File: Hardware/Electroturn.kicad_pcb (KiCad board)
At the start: 2 copper layers, 100 x 100 mm, 10 parts, among them J1 Encoder Terminal, J2 Stepper Motor Terminal, U1 Teensy 4.0, U2 MCP23017_SP

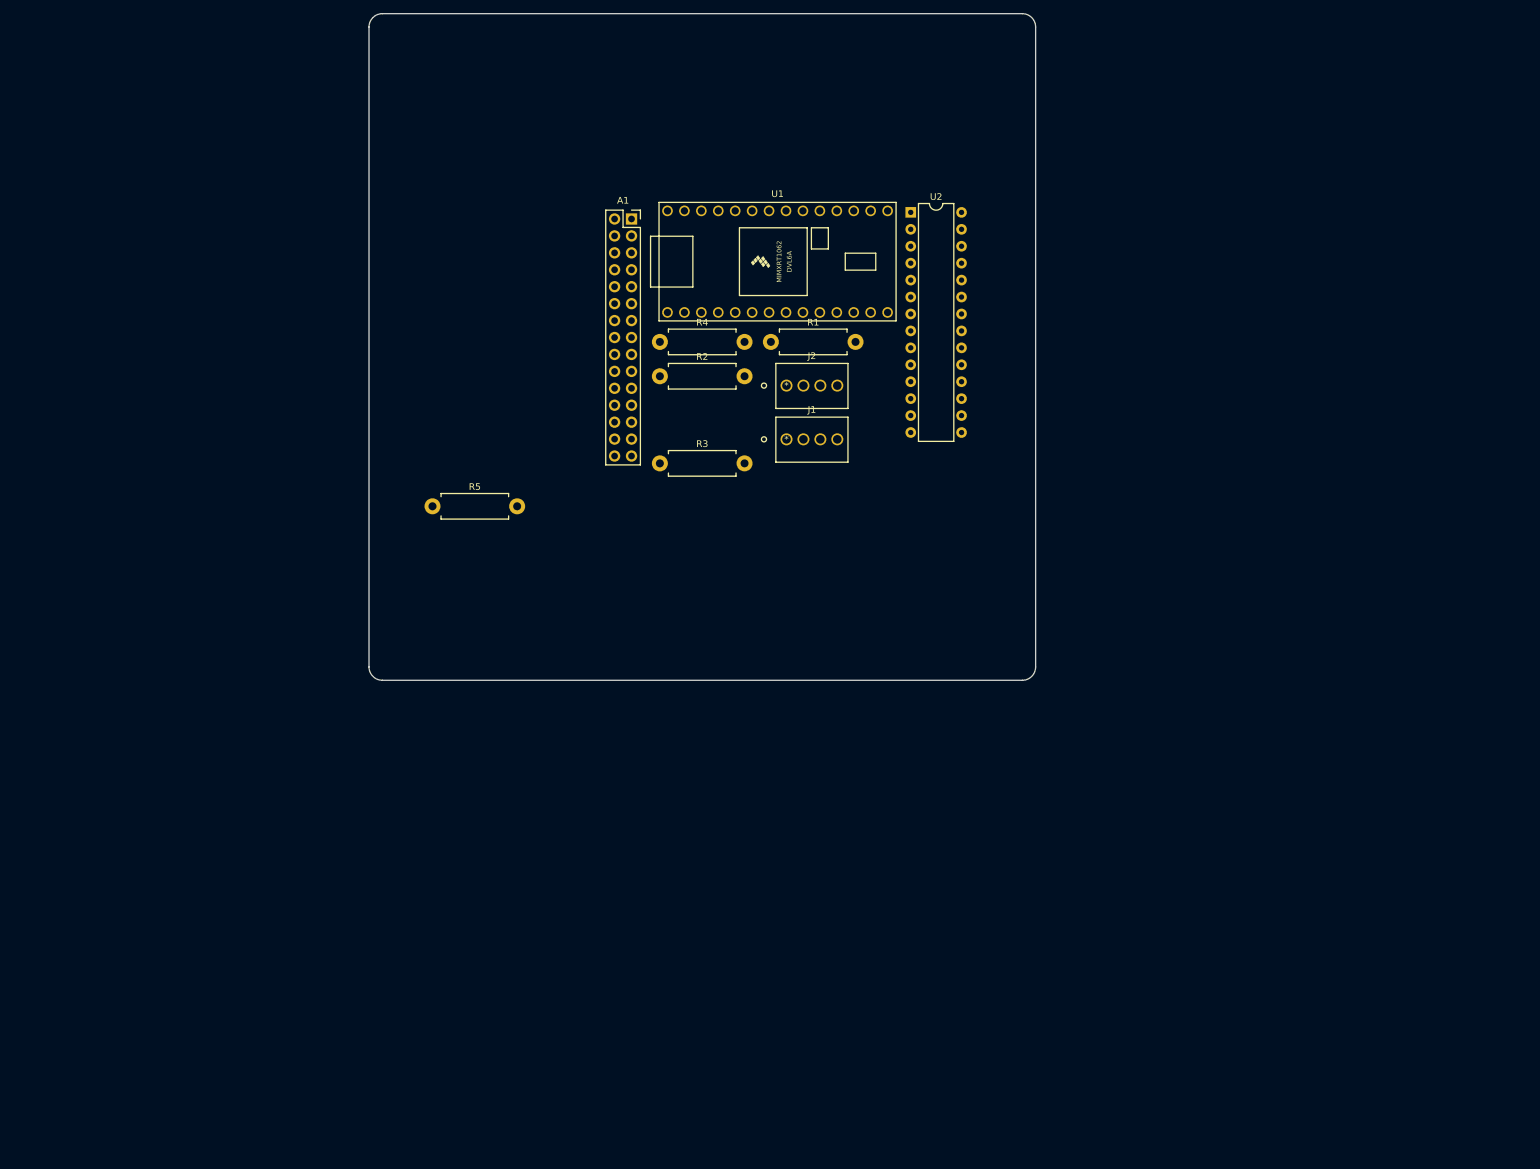
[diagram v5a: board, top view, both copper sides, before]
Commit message: Footprint housekeeping, updating PCB components
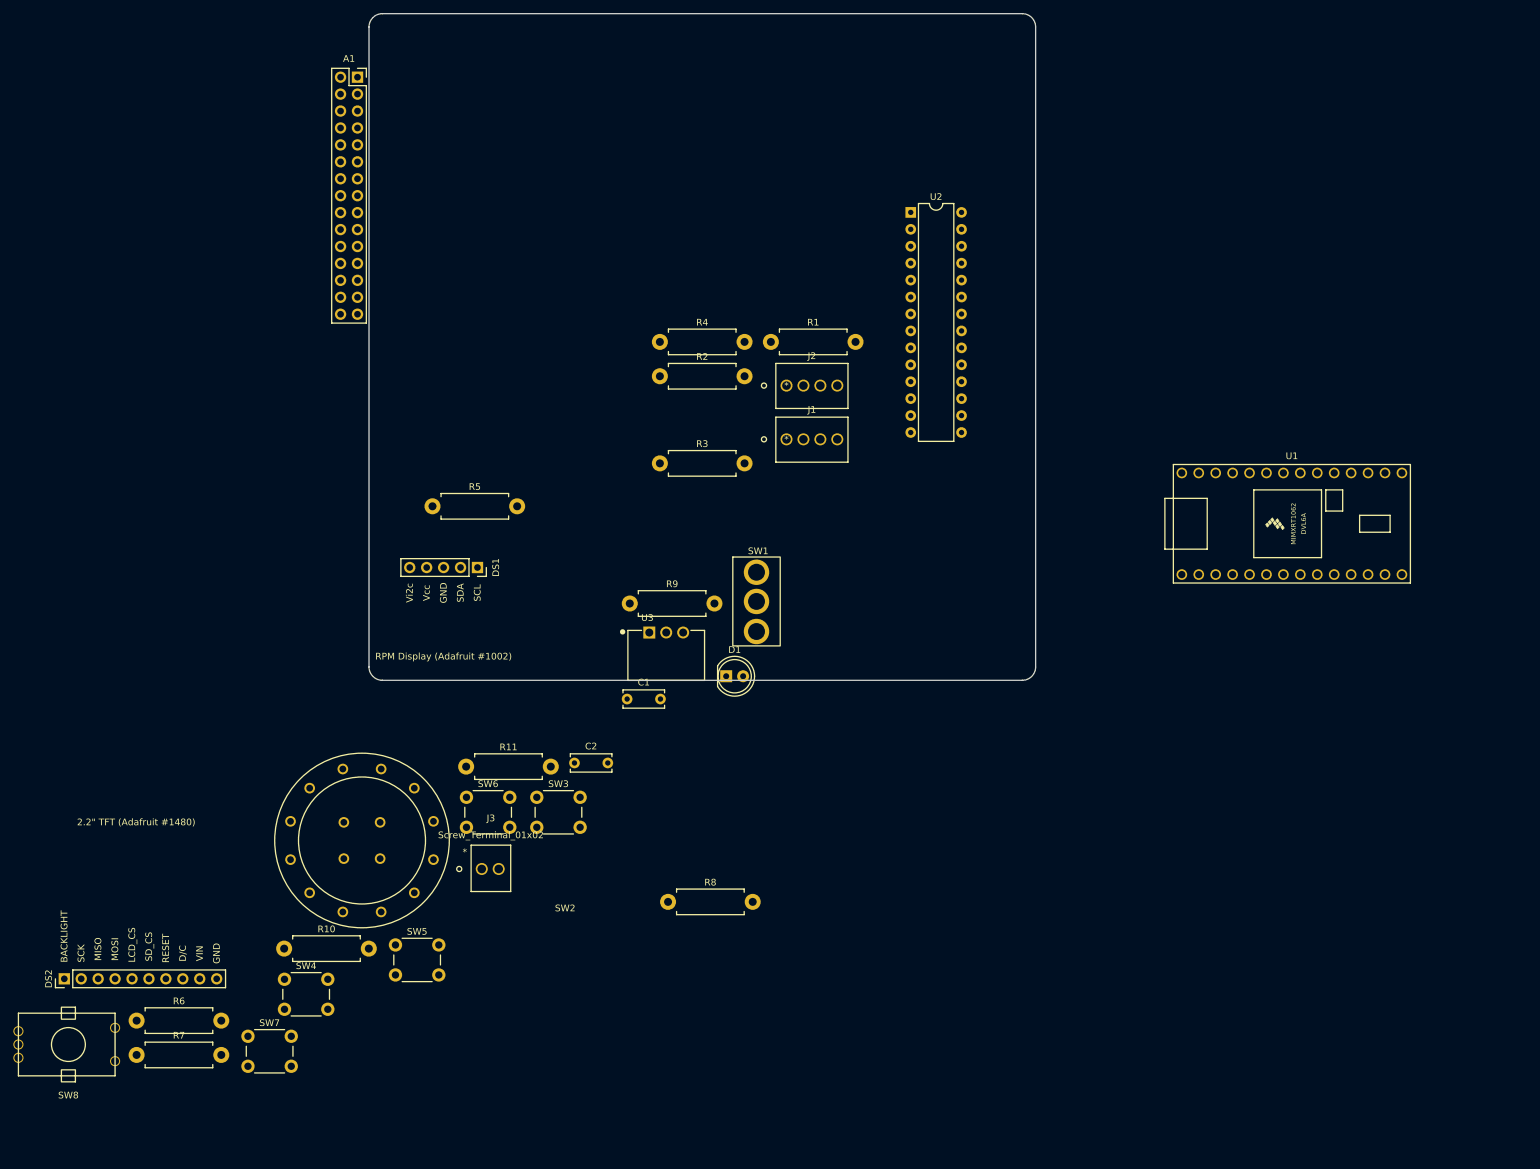
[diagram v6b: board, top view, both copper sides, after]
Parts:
- added C1: 0.01uF, Capacitor_THT:C_Disc_D6.0mm_W2.5mm_P5.00mm, F.Cu at (118.7, 122.8)
- added C2: 0.01uF, Capacitor_THT:C_Disc_D6.0mm_W2.5mm_P5.00mm, F.Cu at (110.8, 132.4)
- added D1: Spindle Overspeed LED, LED_THT:LED_D5.0mm, F.Cu at (133.6, 119.4)
- added DS1: Adafruit_1002_Alphanumeric, Electroturn_Parts:Adafruit1002_0.54inAlphanumericBackpack, F.Cu at (96.3, 103.1)
- added DS2: Adafruit_1480_2.2inTFT, Electroturn_Parts:Adafruit1480_TFTwithHeaders, F.Cu at (34.3, 164.8)
- added J3: Screw_Terminal_01x02, Electroturn_Parts:01x02ScrewTerm_OSTVN02A150, F.Cu at (96.9, 148.3)
- added R10: 10k, Resistor_THT:R_Axial_DIN0411_L9.9mm_D3.6mm_P12.70mm_Horizontal, F.Cu at (67.3, 160.3)
- added R11: 10k, Resistor_THT:R_Axial_DIN0411_L9.9mm_D3.6mm_P12.70mm_Horizontal, F.Cu at (94.6, 133.0)
- added R6: 1.5k, Resistor_THT:R_Axial_DIN0411_L9.9mm_D3.6mm_P12.70mm_Horizontal, F.Cu at (45.1, 171.1)
- added R7: 1.5k, Resistor_THT:R_Axial_DIN0411_L9.9mm_D3.6mm_P12.70mm_Horizontal, F.Cu at (45.1, 176.2)
- added R8: 10k, Resistor_THT:R_Axial_DIN0411_L9.9mm_D3.6mm_P12.70mm_Horizontal, F.Cu at (124.9, 153.2)
- added R9: 10k, Resistor_THT:R_Axial_DIN0411_L9.9mm_D3.6mm_P12.70mm_Horizontal, F.Cu at (119.1, 108.5)
- added SW1: Feed Switch, Electroturn_Parts:SPDT_OnOffOn_ToggleSwitch_fromECEdepartment_CircularPads, F.Cu at (134.6, 101.5)
- added SW2: Motor Braking Switch, Electroturn_Parts:SW_SPDT_CK_ A11405RNZQ, F.Cu at (78.9, 144.0)
- added SW3: Mode Right Scroll, Button_Switch_THT:SW_PUSH_6mm_H9.5mm, F.Cu at (105.2, 137.6)
- added SW4: Mode Left Scroll, Button_Switch_THT:SW_PUSH_6mm_H9.5mm, F.Cu at (67.3, 164.9)
- added SW5: Function Btn 1, Button_Switch_THT:SW_PUSH_6mm_H9.5mm, F.Cu at (84.0, 159.7)
- added SW6: Function Btn 2, Button_Switch_THT:SW_PUSH_6mm_H9.5mm, F.Cu at (94.6, 137.6)
- added SW7: Function Btn 2, Button_Switch_THT:SW_PUSH_6mm_H9.5mm, F.Cu at (61.8, 173.4)
- added SW8: Control Panel Encoder, Electroturn_Parts:CUIDevices_ACZ11BR1E20FD112C, F.Cu at (34.9, 174.6)
- added U3: 5vSwitchingRegulator_VXO7805-1000, Electroturn_Parts:5vSwitchingRegulator_CONV_VXO7805-1000, F.Cu at (122.0, 112.8)
- moved U1 86.6 mm to (218.4, 96.5)
- moved A1 46.3 mm to (78.3, 29.5)
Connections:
- U2 pad 15: unconnected-(U2-Pad15) -> GND
- U2 pad 16: unconnected-(U2-Pad16) -> GND
- U2 pad 17: unconnected-(U2-Pad17) -> GND
- U2 pad 18: unconnected-(U2-Pad18) -> +3V3
